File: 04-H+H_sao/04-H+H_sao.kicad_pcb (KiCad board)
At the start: 2 copper layers, 99 x 90.6 mm, 14 parts, among them U1 ICM7555, X1 Badgelife_sao_connector_v169b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

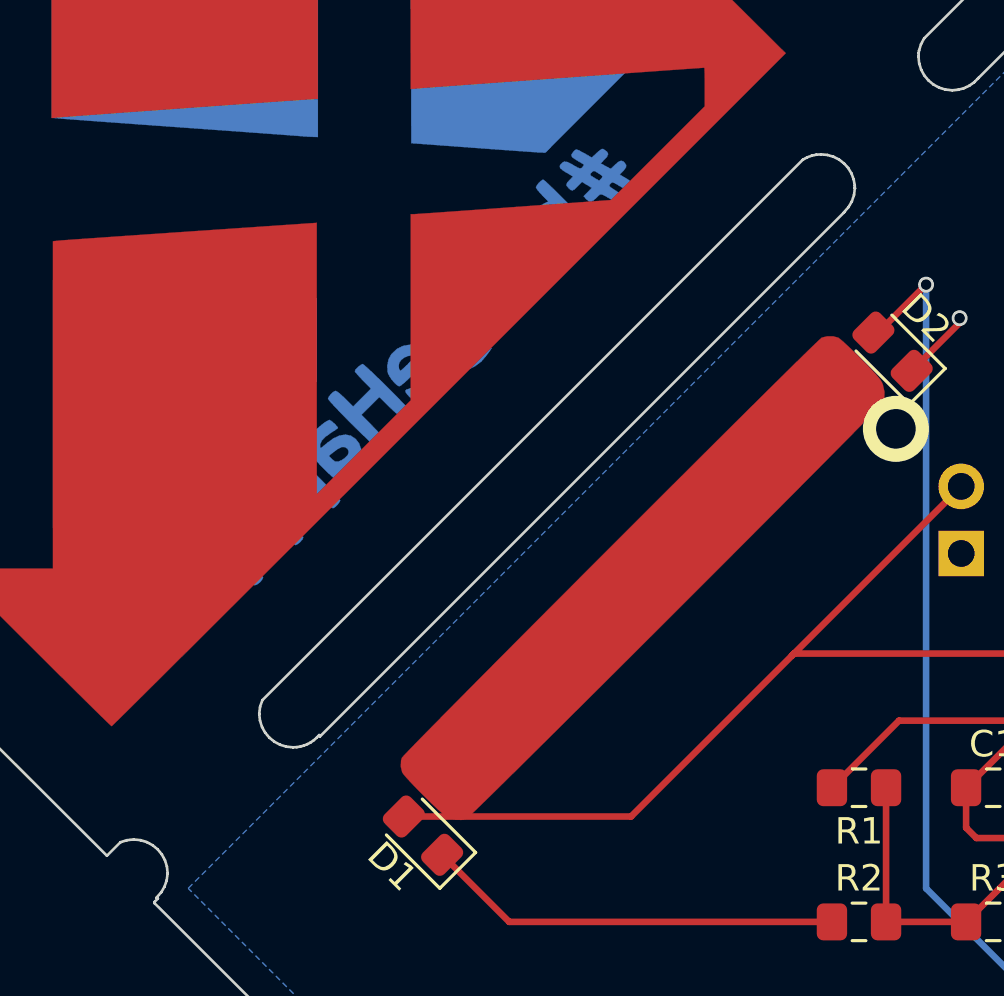
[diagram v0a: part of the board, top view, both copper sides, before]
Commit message: adding b silk making slots smaller
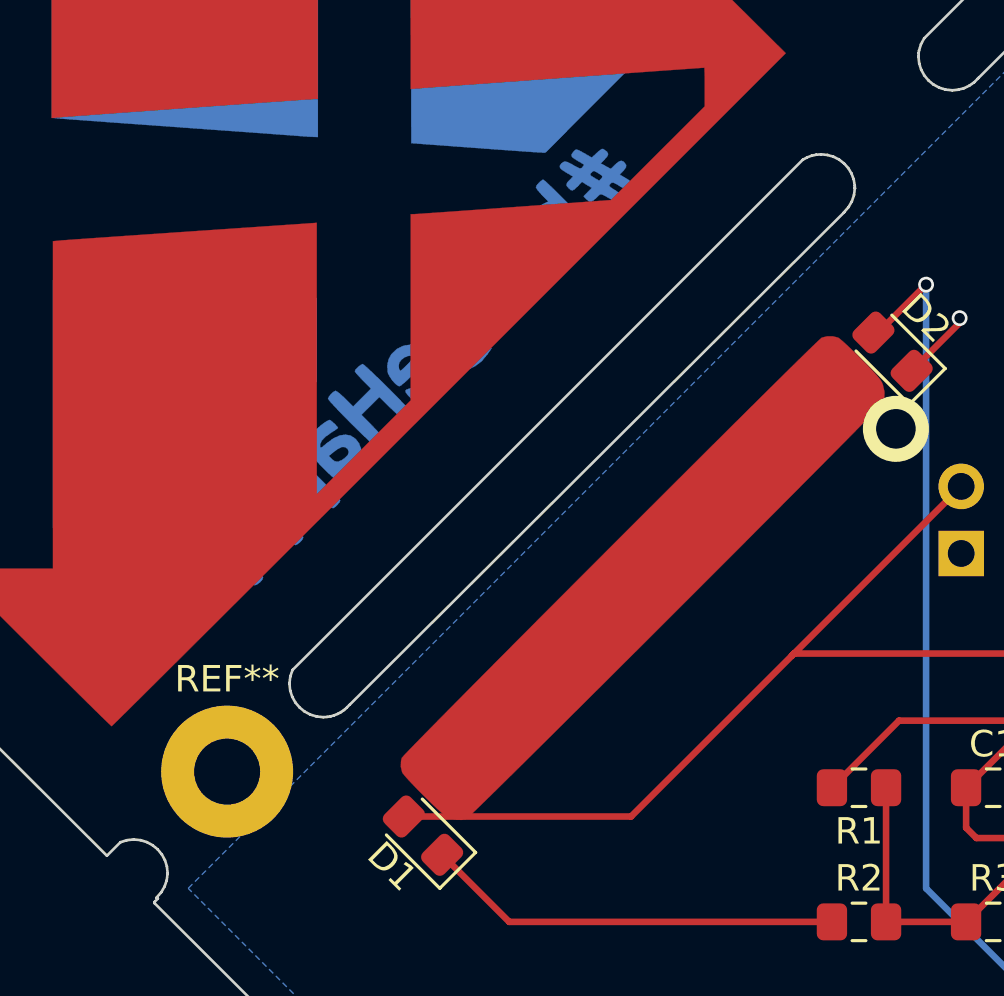
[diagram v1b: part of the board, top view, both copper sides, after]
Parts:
- removed the G*** at (152.4, 95.2) (x4)
- added G*** (x4): LOGO, LOGO, F.Cu at (152.4, 95.2)
- added REF**: MountingHole_2.5mm_Pad, MountingHole:MountingHole_2.5mm_Pad, F.Cu at (122.1, 125.1)
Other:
- outline, holes or cut-outs redrawn
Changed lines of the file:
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@@
   (general
     (thickness 1.6)
-    (drawings 1111)
+    (drawings 1110)
     (tracks 54)
     (zones 0)
-    (modules 14)
+    (modules 15)
     (nets 13)
   )
@@
     (add_net VDD)
   )
+  (module MountingHole:MountingHole_2.5mm_Pad (layer F.Cu)
+    (at 122.1232 125.1204)
+    (descr "Mounting Hole 2.5mm")
+    (tags "mounting hole 2.5mm")
+    (attr virtual)
+    (fp_text reference REF** (at 0 -3.5) (layer F.SilkS)
+      (effects (font (size 1 1) (thickness 0.15)))
+    )
+    (fp_text value MountingHole_2.5mm_Pad (at 0 3.5) (layer F.Fab)
+      (effects (font (size 1 1) (thickness 0.15)))
+    )
+    (fp_circle (center 0 0) (end 2.75 0) (layer F.CrtYd) (width 0.05))
+    (fp_circle (center 0 0) (end 2.5 0) (layer Cmts.User) (width 0.15))
+    (fp_text user %R (at 0.3 0) (layer F.Fab)
+      (effects (font (size 1 1) (thickness 0.15)))
+    )
+    (pad 1 thru_hole circle (at 0 0) (size 5 5) (drill 2.5) (layers *.Cu *.Mask))
+  )
   (module ICM7555IBAZ-T:SOIC127P600X175-8N (layer F.Cu)
     (at 158.75 128.27)
@@
     )
   )
+  (gr_line (start 126.655544 122.696378) (end 126.548931 122.788976) (layer Edge.Cuts) (width 0.1))
   (gr_poly (pts (xy 156.21 124.46) (xy 161.29 124.46) (xy 161.29 132.08) (xy 156.21 132.08)) (layer F.Mask) (width 0.15))
   (gr_line (start 130.385304 140.532595) (end 145.471724 140.532595) (layer Edge.Cuts) (width 0.1))
@@
   (gr_line (start 145.652364 103.746387) (end 145.482054 103.939005) (layer Edge.Cuts) (width 0.1))
   (gr_line (start 145.482054 103.939005) (end 145.487054 103.942005) (layer Edge.Cuts) (width 0.1))
-  (gr_line (start 145.487054 103.942005) (end 125.635554 123.793505) (layer Edge.Cuts) (width 0.1))
-  (gr_line (start 125.635554 123.793505) (end 125.609154 123.734605) (layer Edge.Cuts) (width 0.1))
-  (gr_line (start 125.609154 123.734605) (end 125.512544 123.839378) (layer Edge.Cuts) (width 0.1))
-  (gr_line (start 125.512544 123.839378) (end 125.405931 123.931976) (layer Edge.Cuts) (width 0.1))
-  (gr_line (start 125.405931 123.931976) (end 125.290473 124.011853) (layer Edge.Cuts) (width 0.1))
-  (gr_line (start 125.290473 124.011853) (end 125.167332 124.07846) (layer Edge.Cuts) (width 0.1))
-  (gr_line (start 125.167332 124.07846) (end 125.037664 124.13125) (layer Edge.Cuts) (width 0.1))
-  (gr_line (start 125.037664 124.13125) (end 124.902629 124.169676) (layer Edge.Cuts) (width 0.1))
-  (gr_line (start 124.902629 124.169676) (end 124.763386 124.19319) (layer Edge.Cuts) (width 0.1))
-  (gr_line (start 124.763386 124.19319) (end 124.621094 124.201245) (layer Edge.Cuts) (width 0.1))
-  (gr_line (start 124.621094 124.201245) (end 124.364792 124.17553) (layer Edge.Cuts) (width 0.1))
-  (gr_line (start 124.364792 124.17553) (end 124.125815 124.101889) (layer Edge.Cuts) (width 0.1))
-  (gr_line (start 124.125815 124.101889) (end 123.90923 123.985332) (layer Edge.Cuts) (width 0.1))
-  (gr_line (start 123.90923 123.985332) (end 123.720104 123.830869) (layer Edge.Cuts) (width 0.1))
-  (gr_line (start 123.720104 123.830869) (end 123.563504 123.643508) (layer Edge.Cuts) (width 0.1))
-  (gr_line (start 123.563504 123.643508) (end 123.444496 123.428259) (layer Edge.Cuts) (width 0.1))
-  (gr_line (start 123.444496 123.428259) (end 123.368147 123.190132) (layer Edge.Cuts) (width 0.1))
-  (gr_line (start 123.368147 123.190132) (end 123.339524 122.934135) (layer Edge.Cuts) (width 0.1))
-  (gr_line (start 123.339524 122.934135) (end 123.370483 122.669152) (layer Edge.Cuts) (width 0.1))
-  (gr_line (start 123.370483 122.669152) (end 123.455794 122.416335) (layer Edge.Cuts) (width 0.1))
-  (gr_line (start 123.455794 122.416335) (end 123.456314 122.415335) (layer Edge.Cuts) (width 0.1))
-  (gr_line (start 123.456314 122.415335) (end 143.919664 101.952505) (layer Edge.Cuts) (width 0.1))
+  (gr_line (start 145.487054 103.942005) (end 126.7714 122.5804) (layer Edge.Cuts) (width 0.1))
+  (gr_line (start 126.752154 122.591605) (end 126.655544 122.696378) (layer Edge.Cuts) (width 0.1))
+  (gr_line (start 126.548931 122.788976) (end 126.433473 122.868853) (layer Edge.Cuts) (width 0.1))
+  (gr_line (start 126.433473 122.868853) (end 126.310332 122.93546) (layer Edge.Cuts) (width 0.1))
+  (gr_line (start 126.310332 122.93546) (end 126.180664 122.98825) (layer Edge.Cuts) (width 0.1))
+  (gr_line (start 126.180664 122.98825) (end 126.045629 123.026676) (layer Edge.Cuts) (width 0.1))
+  (gr_line (start 126.045629 123.026676) (end 125.906386 123.05019) (layer Edge.Cuts) (width 0.1))
+  (gr_line (start 125.906386 123.05019) (end 125.764094 123.058245) (layer Edge.Cuts) (width 0.1))
+  (gr_line (start 125.764094 123.058245) (end 125.507792 123.03253) (layer Edge.Cuts) (width 0.1))
+  (gr_line (start 125.507792 123.03253) (end 125.268815 122.958889) (layer Edge.Cuts) (width 0.1))
+  (gr_line (start 125.268815 122.958889) (end 125.05223 122.842332) (layer Edge.Cuts) (width 0.1))
+  (gr_line (start 125.05223 122.842332) (end 124.863104 122.687869) (layer Edge.Cuts) (width 0.1))
+  (gr_line (start 124.863104 122.687869) (end 124.706504 122.500508) (layer Edge.Cuts) (width 0.1))
+  (gr_line (start 124.706504 122.500508) (end 124.587496 122.285259) (layer Edge.Cuts) (width 0.1))
+  (gr_line (start 124.587496 122.285259) (end 124.511147 122.047132) (layer Edge.Cuts) (width 0.1))
+  (gr_line (start 124.511147 122.047132) (end 124.482524 121.791135) (layer Edge.Cuts) (width 0.1))
+  (gr_line (start 124.482524 121.791135) (end 124.513483 121.526152) (layer Edge.Cuts) (width 0.1))
+  (gr_line (start 124.513483 121.526152) (end 124.598794 121.273335) (layer Edge.Cuts) (width 0.1))
+  (gr_line (start 124.598794 121.273335) (end 124.599314 121.272335) (layer Edge.Cuts) (width 0.1))
+  (gr_line (start 124.587 121.285) (end 143.919664 101.952505) (layer Edge.Cuts) (width 0.1))
   (gr_line (start 143.919664 101.952505) (end 144.080145 101.864394) (layer Edge.Cuts) (width 0.1))
   (gr_line (start 144.080145 101.864394) (end 144.250656 101.800301) (layer Edge.Cuts) (width 0.1))

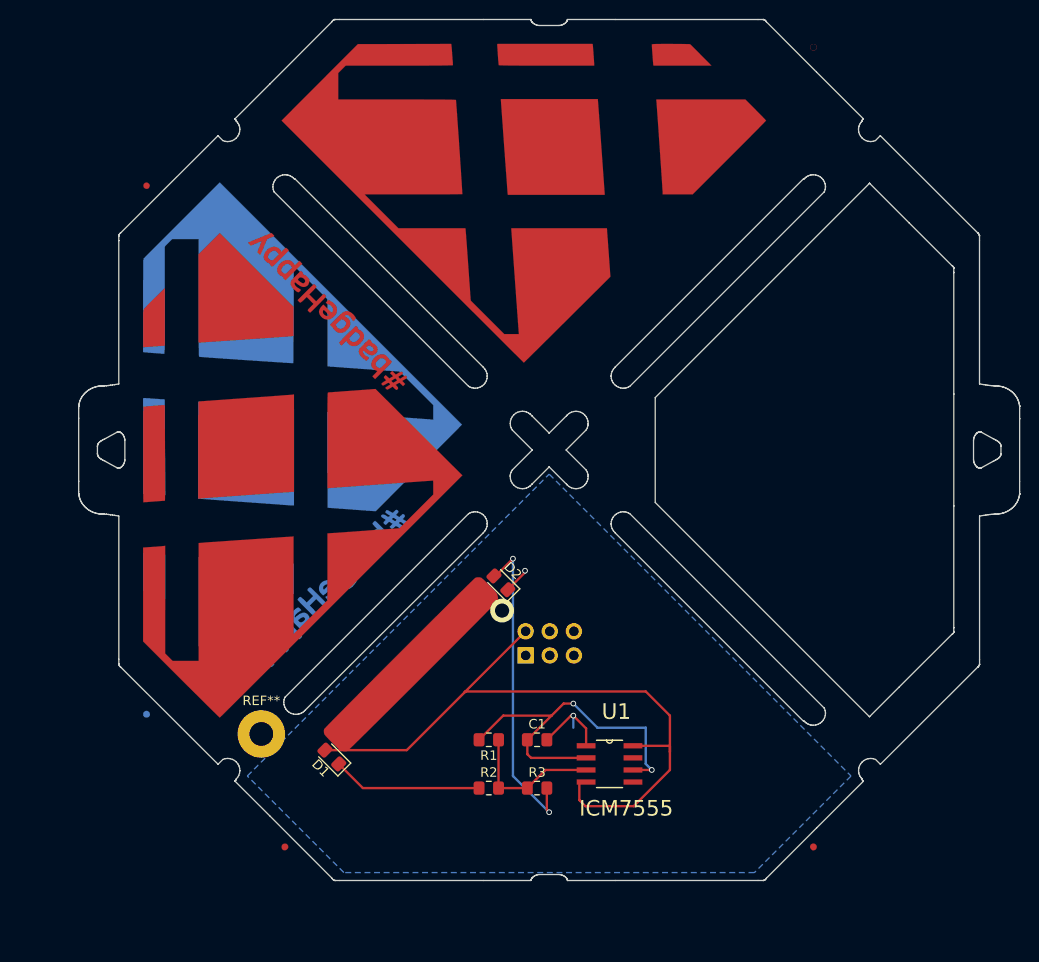
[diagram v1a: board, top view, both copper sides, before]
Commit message: rerouted sao
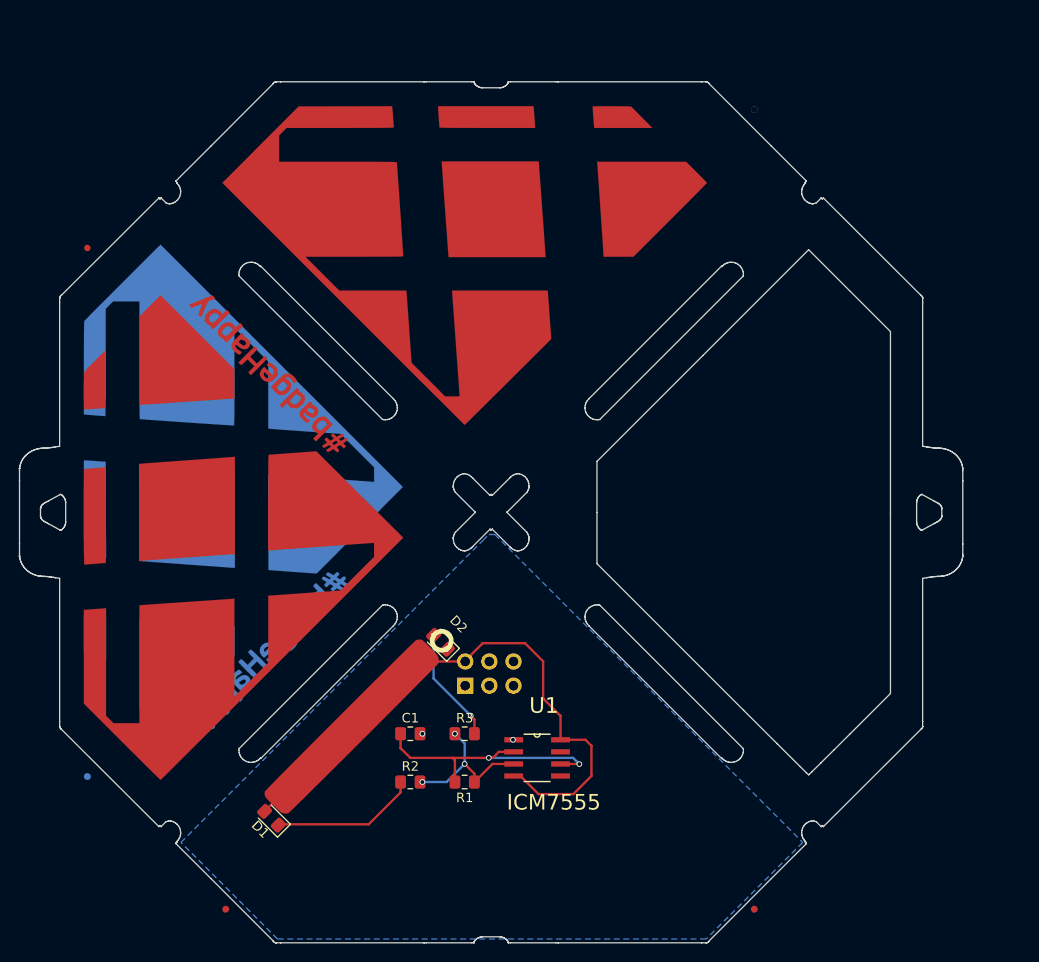
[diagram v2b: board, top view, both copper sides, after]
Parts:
- removed the G*** at (152.4, 95.2) (x4)
- removed REF**: MountingHole_2.5mm_Pad, MountingHole:MountingHole_2.5mm_Pad
- added G*** (x5): LOGO, LOGO, F.Cu at (146.2, 101.8)
- moved C1 13.4 mm to (137.8, 125.1)
- moved R3 9.53 mm to (143.5, 125.1)
- moved D1 9.04 mm to (123.2, 134.0)
- moved ? 9.04 mm to (174.0, 59.4)
- moved D2 8.92 mm to (141.0, 115.5)
- moved R2 8.28 mm to (137.8, 130.2)
- moved U1 7.65 mm to (151.1, 127.6)
- moved X1 7.10 mm to (146.1, 118.7)
- moved R1 5.12 mm to (143.5, 130.2)
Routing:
- net Net-(D2-Pad2): track 33.6 -> 12.1 mm
- net GND: track 11.6 -> 0.00 mm, vias 2 -> 3
- net VDD: track 73.7 -> 62.9 mm
- net Drain: track 38.3 -> 28.5 mm
- net Net-(R1-Pad1): track 15.1 -> 16.8 mm, vias 0 -> 3
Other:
- board size 99 x 90.6 mm -> 99.2 x 90.6 mm
